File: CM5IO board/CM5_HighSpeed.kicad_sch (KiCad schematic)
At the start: 18 parts, among them J10 690-019-298-412, J12 USB3_A, J16 Conn_01x22_Female, J5 Conn_01x22_Female, J6 THD-02-R, U12 RT9742SNGV, U6 AP22653W6

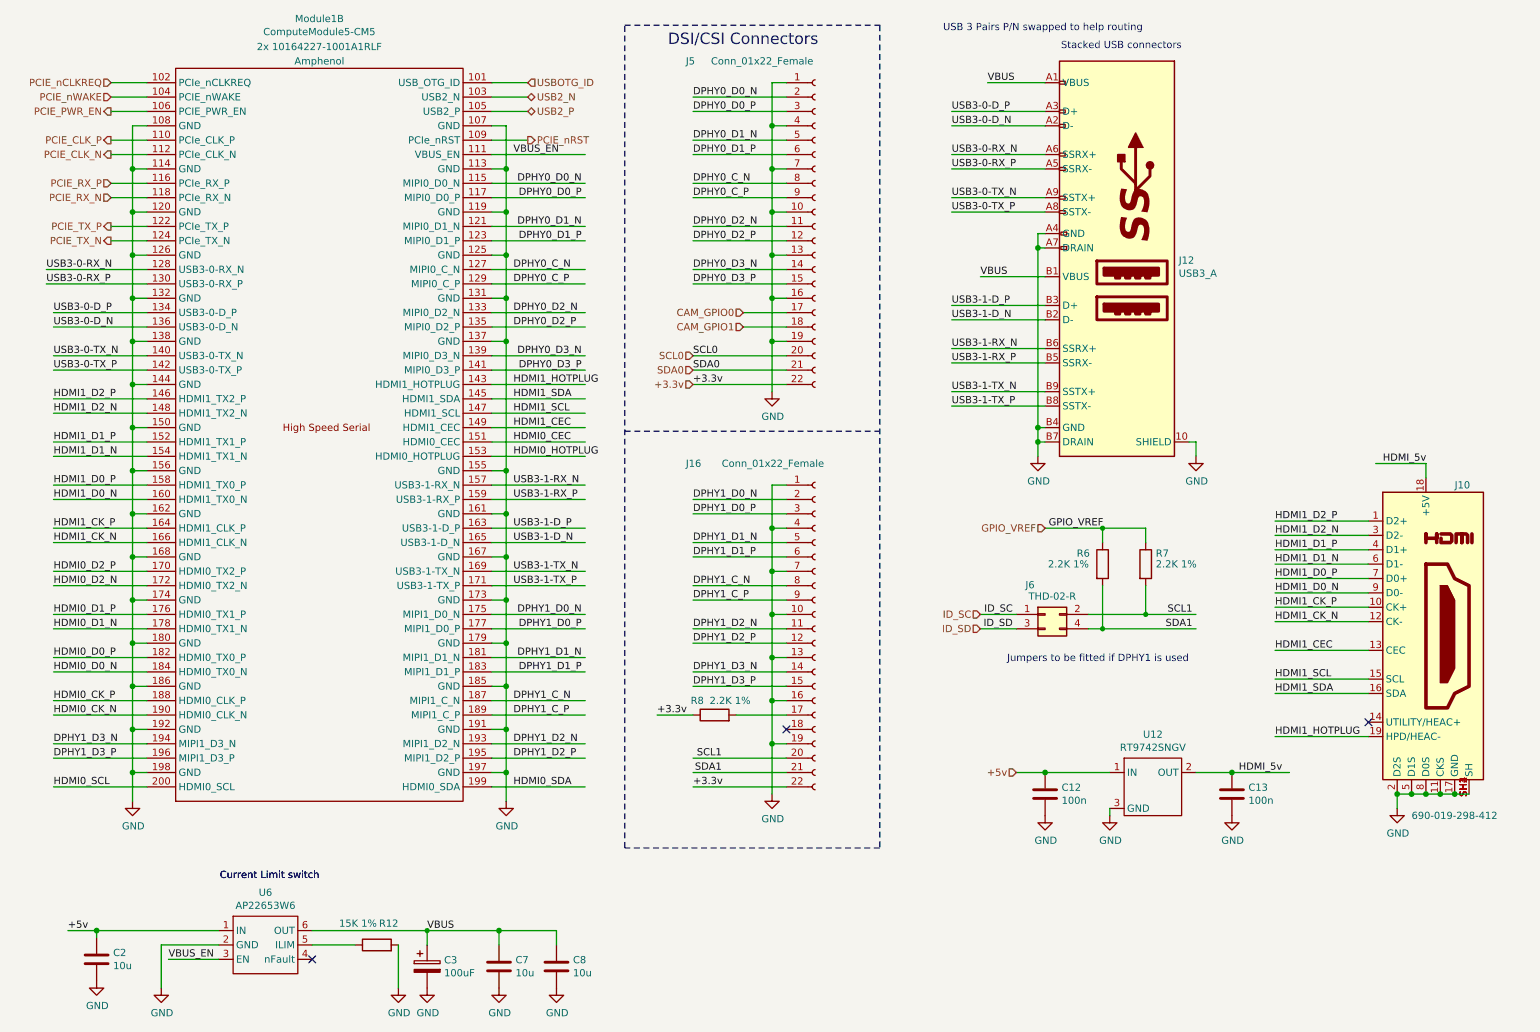
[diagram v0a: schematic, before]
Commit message: Moved CM5IO folder; Removed Ethernet, Battery (successfully?)
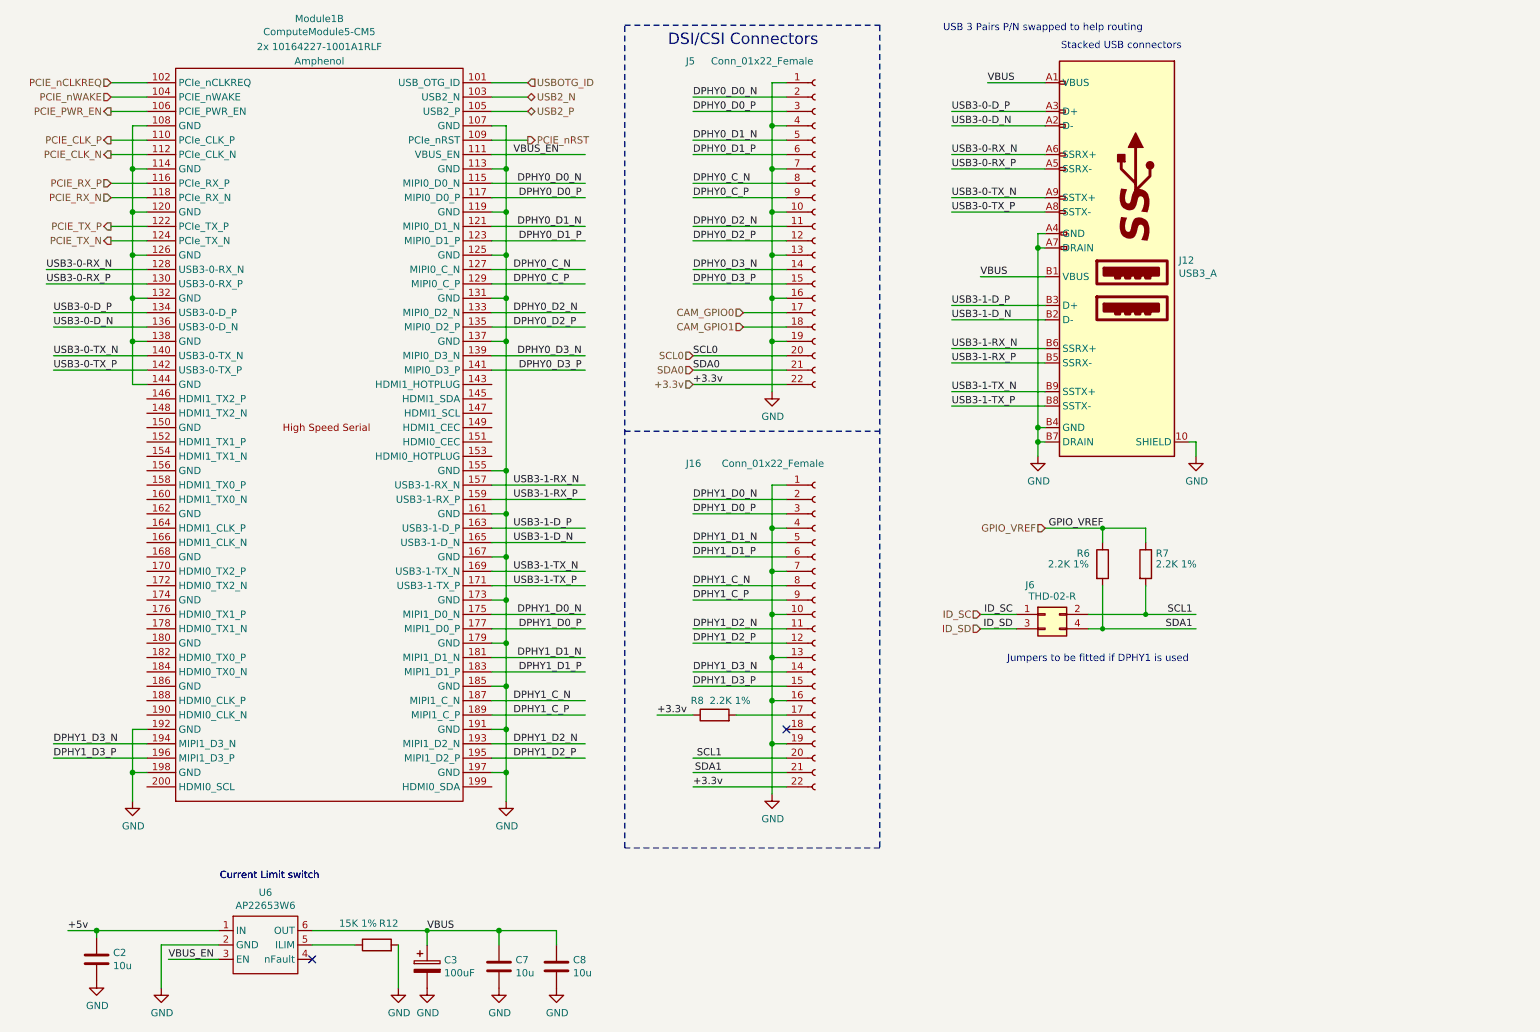
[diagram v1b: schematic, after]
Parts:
- removed C12, C13: 100n, Capacitor_SMD:C_0402_1005Metric, symbol Device:C
- removed J10: 690-019-298-412, CM5IO:EDAC 690-019-298-412, symbol CM5IO:HDMI_A_1.4
- removed U12: RT9742SNGV, Package_TO_SOT_SMD:TSOT-23_HandSoldering, symbol CM5IO:RT9742SNGV
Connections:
- net GND: no longer Module1.108 (GND), Module1.114 (GND), Module1.120 (GND), Module1.126 (GND), Module1.132 (GND), Module1.138 (GND), Module1.144 (GND), Module1.150 (GND), Module1.156 (GND), Module1.162 (GND), Module1.168 (GND), Module1.174 (GND), Module1.180 (GND), Module1.186 (GND)
- net HDMI0_CEC: no longer names the net of Module1.151 (HDMI0_CEC)
- net HDMI0_CK_N: no longer names the net of Module1.190 (HDMI0_CLK_N)
- net HDMI0_CK_P: no longer names the net of Module1.188 (HDMI0_CLK_P)
- net HDMI0_D0_N: no longer names the net of Module1.184 (HDMI0_TX0_N)
- net HDMI0_D0_P: no longer names the net of Module1.182 (HDMI0_TX0_P)
- net HDMI0_D1_N: no longer names the net of Module1.178 (HDMI0_TX1_N)
- net HDMI0_D1_P: no longer names the net of Module1.176 (HDMI0_TX1_P)
- net HDMI0_D2_N: no longer names the net of Module1.172 (HDMI0_TX2_N)
- net HDMI0_D2_P: no longer names the net of Module1.170 (HDMI0_TX2_P)
- net HDMI0_HOTPLUG: no longer names the net of Module1.153 (HDMI0_HOTPLUG)
- net HDMI0_SCL: no longer names the net of Module1.200 (HDMI0_SCL)
- net HDMI0_SDA: no longer names the net of Module1.199 (HDMI0_SDA)
- net HDMI1_CEC: no longer names the net of Module1.149 (HDMI1_CEC)
- net HDMI1_CK_N: no longer names the net of Module1.166 (HDMI1_CLK_N)
- net HDMI1_CK_P: no longer names the net of Module1.164 (HDMI1_CLK_P)
- net HDMI1_D0_N: no longer names the net of Module1.160 (HDMI1_TX0_N)
- net HDMI1_D0_P: no longer names the net of Module1.158 (HDMI1_TX0_P)
- net HDMI1_D1_N: no longer names the net of Module1.154 (HDMI1_TX1_N)
- net HDMI1_D1_P: no longer names the net of Module1.152 (HDMI1_TX1_P)
- net HDMI1_D2_N: no longer names the net of Module1.148 (HDMI1_TX2_N)
- net HDMI1_D2_P: no longer names the net of Module1.146 (HDMI1_TX2_P)
- net HDMI1_HOTPLUG: no longer names the net of Module1.143 (HDMI1_HOTPLUG)
- net HDMI1_SCL: no longer names the net of Module1.147 (HDMI1_SCL)
- net HDMI1_SDA: no longer names the net of Module1.145 (HDMI1_SDA)
- new net: Module1.108 (GND), Module1.114 (GND), Module1.120 (GND), Module1.126 (GND), Module1.132 (GND), Module1.138 (GND), Module1.144 (GND)
- no-connect marks 3 -> 2

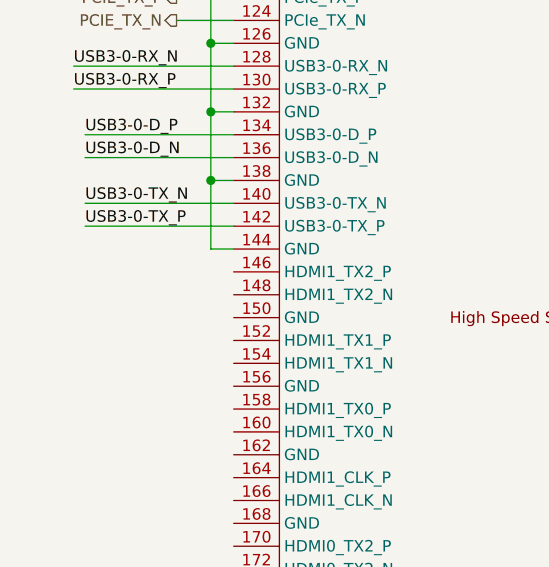
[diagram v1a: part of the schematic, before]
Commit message: Duplicated additional USB-C in sch.
How to change pin label on CM5?
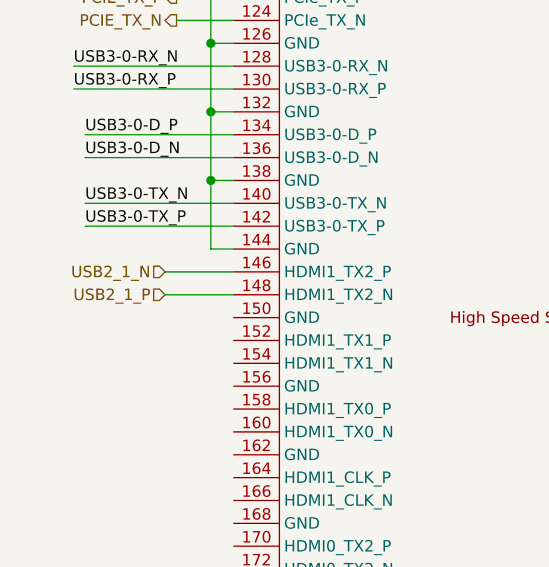
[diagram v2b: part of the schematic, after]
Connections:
- net USB2_1_N: now reaches Module1.146 (HDMI1_TX2_P)
- net USB2_1_P: now reaches Module1.148 (HDMI1_TX2_N)
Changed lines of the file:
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@@
+	(wire
+		(pts
+			(xy 30.48 83.82) (xy 38.1 83.82)
+		)
+		(stroke
+			(width 0)
+			(type default)
+		)
+	)
 	(wire
 		(pts
@@
 			(width 0)
 			(type solid)
+		)
+	)
+	(wire
+		(pts
+			(xy 30.48 81.28) (xy 38.1 81.28)
+		)
+		(stroke
+			(width 0)
+			(type default)
 		)
 	)
@@
 		)
 	)
+	(hierarchical_label "USB2_1_P"
+		(shape input)
+		(at 30.48 83.82 180)
+		(effects
+			(font
+				(size 1.27 1.27)
+			)
+			(justify right)
+		)
+	)
 	(hierarchical_label "CAM_GPIO0"
 		(shape input)
@@
 		(effects
 			(font
+				(size 1.27 1.27)
+			)
+			(justify right)
+		)
+	)
+	(hierarchical_label "USB2_1_N"
+		(shape input)
+		(at 30.48 81.28 180)
+		(effects
+			(font

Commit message: Added "Buck Boost" hierarchical sheet; Deleted two USB-C ports
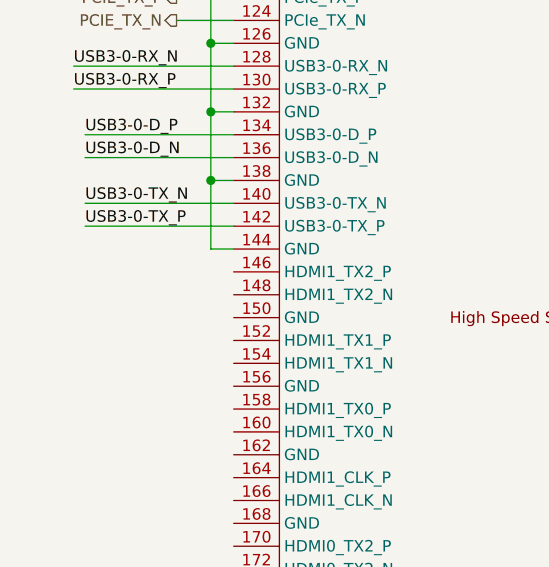
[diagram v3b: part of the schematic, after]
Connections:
- net USB2_1_N: no longer names the net of Module1.146 (HDMI1_TX2_P)
- net USB2_1_P: no longer names the net of Module1.148 (HDMI1_TX2_N)
